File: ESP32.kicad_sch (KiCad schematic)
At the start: 33 parts, among them J2 Conn_01x04_Socket, U2 ESP32-C3FH4, U4 TS-1187A-B-A-B, U58 TS-1187A-B-A-B, U59 YTC-TC16-30, U60 AMS1117-3_3, X1 CF4040M00015001

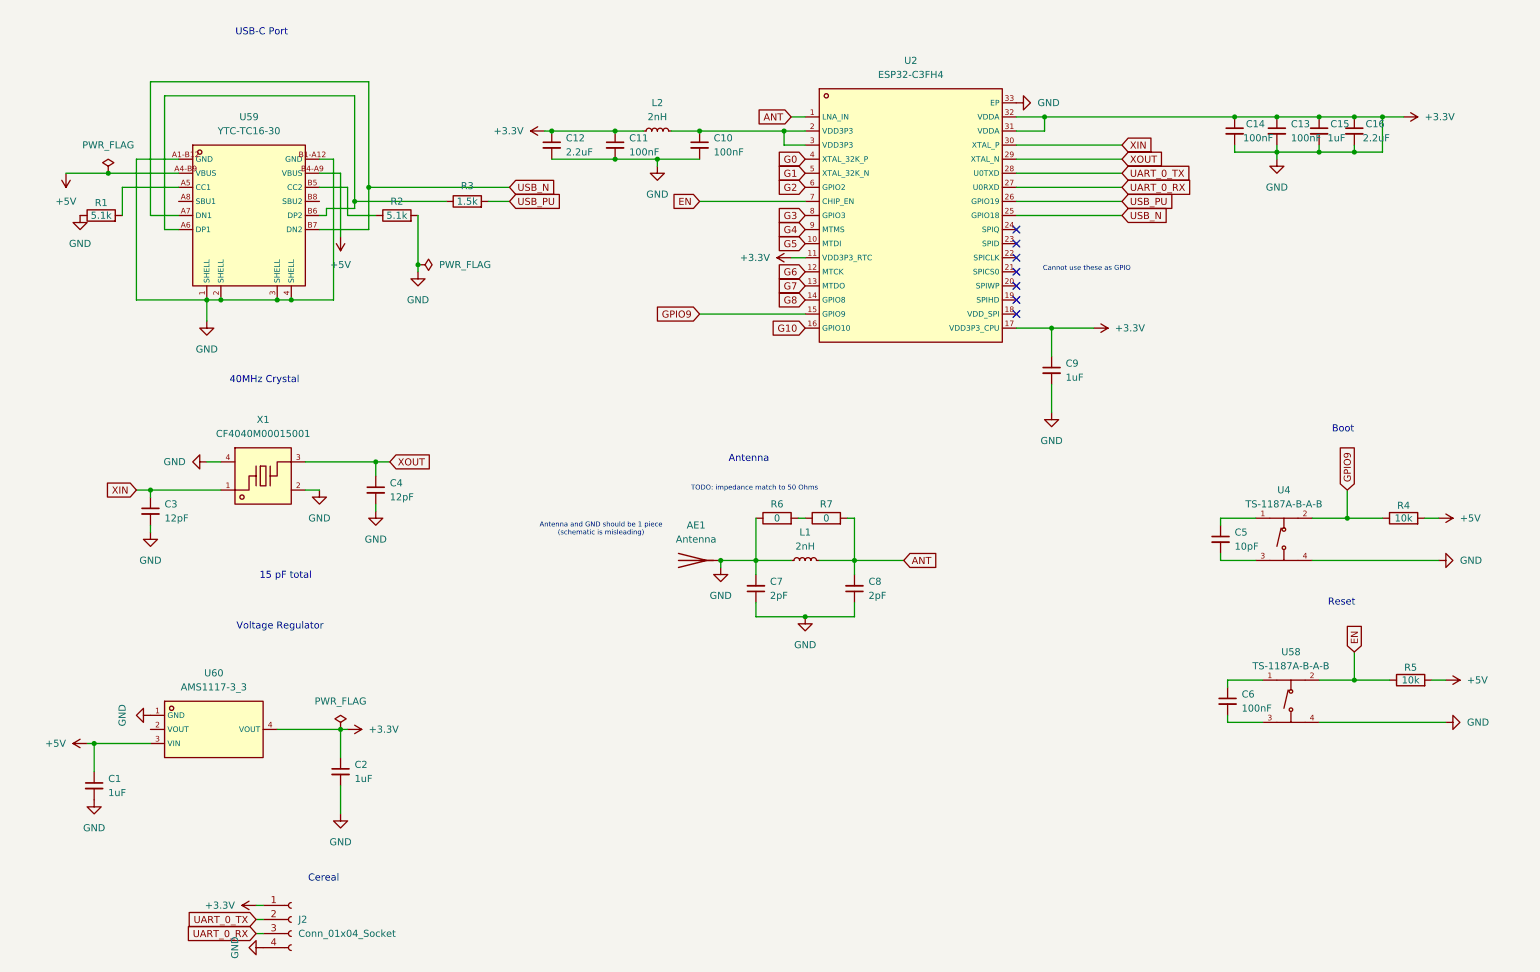
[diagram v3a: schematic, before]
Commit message: symbol fixes + placement
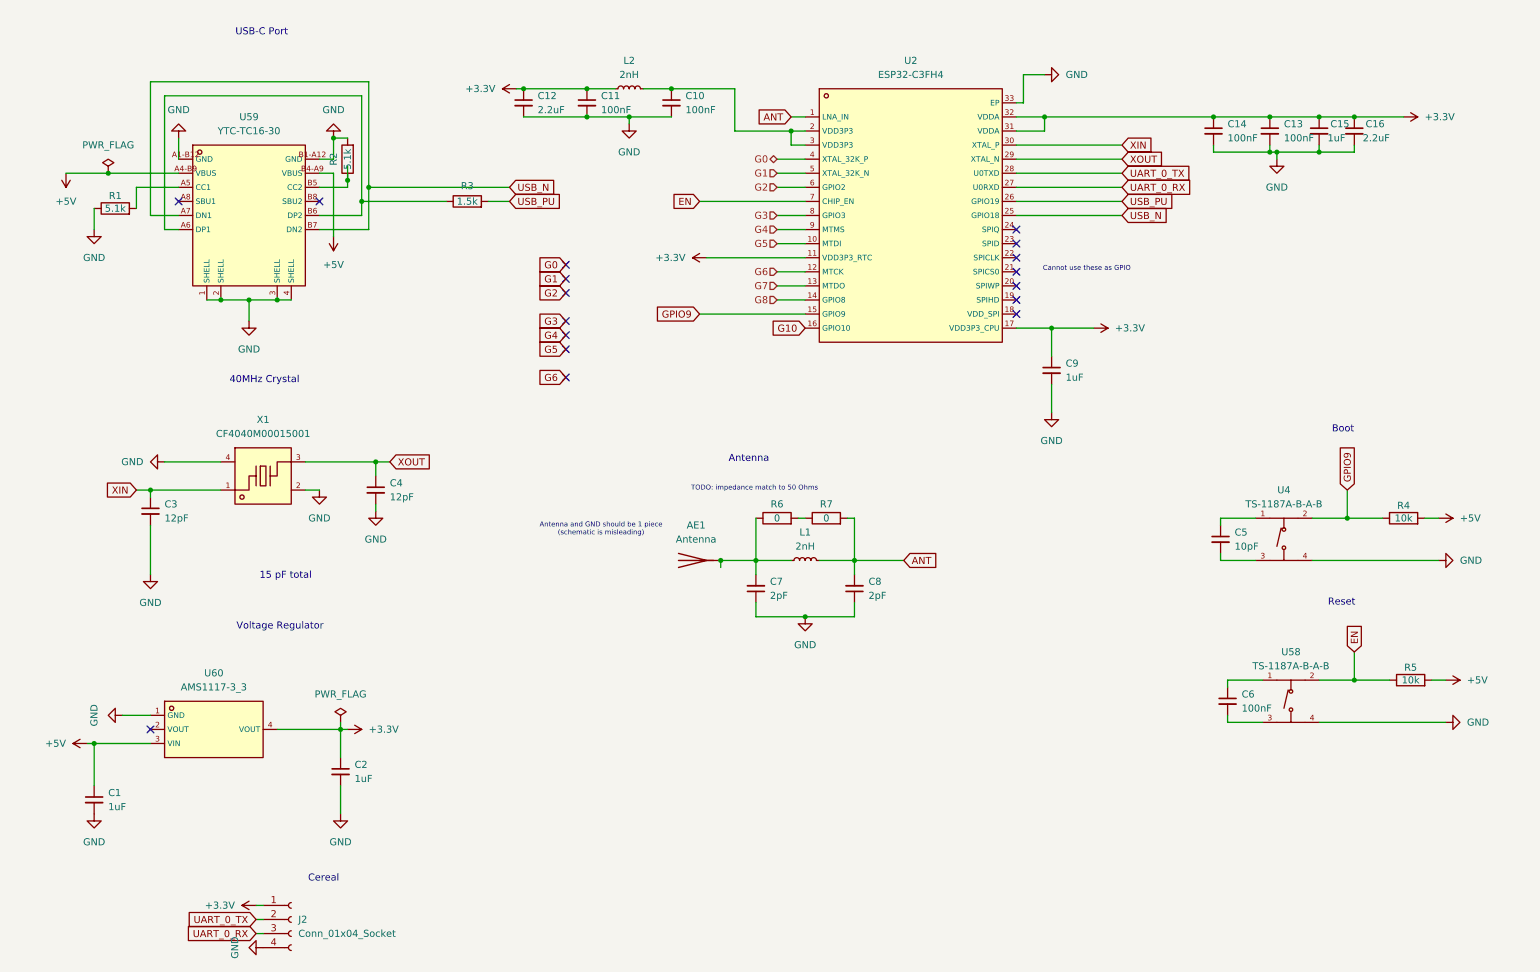
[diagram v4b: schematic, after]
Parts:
- AE1: footprint (none) -> ESP_Antenna:ESPRESSIF_ESP32_MIFA_2.4GHz_Right
- C1, C10, C11, C12, C13, C14, C15, C16, C2, C3, C4, C5, C6, C7, C8, C9: footprint (none) -> Capacitor_SMD:C_0402_1005Metric
- J2: footprint (none) -> Connector_PinHeader_2.54mm:PinHeader_1x04_P2.54mm_Vertical
- L1, L2: footprint (none) -> Inductor_SMD:L_0402_1005Metric
- R1, R2, R3, R4, R5, R6, R7: footprint (none) -> Resistor_SMD:R_0402_1005Metric
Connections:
- net +3.3V: no longer AE1.1 (A), C1.2, C10.2, C11.2, C12.2, C13.2, C14.2, C15.2, C16.2, C2.2, C3.2, C4.2, C7.1, C7.2, C8.1, C9.2, J2.4 (Pin_4), L1.1, R1.1, R2.2, R6.1, U2.33 (EP), U4.4 (D), U58.4 (D), U59.1 (SHELL), U59.2 (SHELL), U59.3 (SHELL), U59.4 (SHELL), U59.A1-B12 (GND), U59.B1-A12 (GND), U60.1 (GND), X1.2 (GND), X1.4 (GND)
- new net: AE1.1 (A), C7.2, L1.1, R6.1
- new net GND: C1.2, C10.2, C11.2, C12.2, C13.2, C14.2, C15.2, C16.2, C2.2, C3.2, C4.2, C7.1, C8.1, C9.2, J2.4 (Pin_4), R1.1, R2.2, U2.33 (EP), U4.4 (D), U58.4 (D), U59.1 (SHELL), U59.2 (SHELL), U59.3 (SHELL), U59.4 (SHELL), U59.A1-B12 (GND), U59.B1-A12 (GND), U60.1 (GND), X1.2 (GND), X1.4 (GND)
- no-connect marks 7 -> 17
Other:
- moved on the sheet: C1, C10, C12, L2, R1, R2

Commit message: Add PB_2, PB_8, switch antenna symbol to antenna shield
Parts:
- added C17, C18: 100nF, Capacitor_SMD:C_0402_1005Metric, symbol Device:C_Small
- added R8, R9: 10k, Resistor_SMD:R_0402_1005Metric, symbol Device:R
- added U5, U73: TS-1187A-B-A-B, footprint:SW-SMD_4P-L5.1-W5.1-P3.70-LS6.5-TL-2, symbol TS-1187A-B-A-B:TS-1187A-B-A-B
- AE1: symbol Device:Antenna -> Device:Antenna_Shield
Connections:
- net +5V: now also R8.2, R9.2
- net G2: no longer U2.6 (GPIO2)
- net GND: now also AE1.2 (Shield), U5.4 (D), U73.4 (D)
- net G8 renamed GPIO8
- net GPIO8: now also R9.1, U73.2 (B)
- new net: C18.1, U73.1 (A)
- new net: C18.2, U73.3 (C)
- new net: C17.1, U5.1 (A)
- new net: C17.2, U5.3 (C)
- new net GPIO2: R8.1, U2.6 (GPIO2), U5.2 (B)
- no-connect marks 17 -> 18
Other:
- note added: "PB_2"
- note added: "PB_8"
- note added: "Switches"
- moved on the sheet: C5, C6, R4, R5, U4, U58

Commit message: fixed LED matrix
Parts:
- added D1, D2: D, symbol Device:D
- added L3: 3.9nH, Inductor_SMD:L_0402_1005Metric, symbol Device:L_Small
- L2: value 2nH -> 3.9nH
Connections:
- net G7 is gone; now on net G6: U2.13 (MTDO)
- net +3.3V: now also D1.2 (A), L3.1; no longer U2.31 (VDDA), U2.32 (VDDA)
- net G2: now also U2.8 (GPIO3)
- net G3: now also U2.9 (MTMS); no longer U2.8 (GPIO3)
- net G4: now also U2.10 (MTDI); no longer U2.9 (MTMS)
- net G5: now also U2.12 (MTCK); no longer U2.10 (MTDI)
- net G6: no longer U2.12 (MTCK)
- net at C10.1, L2.2: now also D2.2 (A), L3.2; no longer U2.2 (VDD3P3), U2.3 (VDD3P3)
- new net: D1.1 (K), U2.31 (VDDA), U2.32 (VDDA)
- new net: D2.1 (K), U2.2 (VDD3P3), U2.3 (VDD3P3)
- no-connect marks 18 -> 10

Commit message: fixed LED matrix
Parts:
- removed D1: D, symbol Device:D
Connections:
- net +3.3V: now also U2.31 (VDDA), U2.32 (VDDA)
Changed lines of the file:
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@@
 	(wire
 		(pts
-			(xy 209.55 35.56) (xy 226.06 35.56)
-		)
-		(stroke
-			(width 0)
-			(type default)
-		)
-	)
-	(wire
-		(pts
 			(xy 52.07 68.58) (xy 52.07 72.39)
 		)
@@
 	(wire
 		(pts
-			(xy 195.58 35.56) (xy 201.93 35.56)
+			(xy 195.58 35.56) (xy 226.06 35.56)
 		)
 		(stroke
@@
 					(unit 1)
 				)
-			)
-		)
-	)
-	(symbol
-		(lib_id "Device:D")
-		(at 205.74 35.56 0)
-		(unit 1)
-		(exclude_from_sim no)
-		(in_bom yes)
-		(on_board yes)
-		(dnp no)
-		(fields_autoplaced yes)
-		(property "Reference" "D1"
-			(at 205.74 29.21 0)
-			(effects
-				(font
-					(size 1.27 1.27)
-				)
-			)
-		)
-		(property "Value" "D"
-			(at 205.74 31.75 0)
-			(effects
-				(font
-					(size 1.27 1.27)
-				)
-			)
-		)
-		(property "Footprint" ""
-			(at 205.74 35.56 0)
-			(effects
-				(font
-					(size 1.27 1.27)
-				)
-				(hide yes)
-			)
-		)
-		(property "Datasheet" "~"
-			(at 205.74 35.56 0)
-			(effects
-				(font
-					(size 1.27 1.27)
-				)
-				(hide yes)
-			)
-		)
-		(property "Description" "Diode"
-			(at 205.74 35.56 0)
-			(effects
-				(font
-					(size 1.27 1.27)
-				)
-				(hide yes)
-			)
-		)
-		(property "Sim.Device" "D"
-			(at 205.74 35.56 0)
-			(effects
-				(font
-					(size 1.27 1.27)
-				)
-				(hide yes)
-			)
-		)
-		(property "Sim.Pins" "1=K 2=A"
-			(at 205.74 35.56 0)
-			(effects
-				(font
-					(size 1.27 1.27)
-				)
-				(hide yes)
-			)
-		)
-		(pin "1"
-		)
-		(pin "2"
-		)
-		(instances
-			(project "esp-card"
-				(path "/93cf1a11-1660-4ae3-a523-02ca090cff0a/bb5d4e4a-cd64-4c06-bd3c-c3b86fee81c9"
-					(reference "D1")
-					(unit 1)
-				)

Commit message: better routing
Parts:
- removed D2: D, symbol Device:D
- L1: value 2nH -> 2.2nH
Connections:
- net at C10.1, L2.2, L3.2: now also U2.2 (VDD3P3), U2.3 (VDD3P3)
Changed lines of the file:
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@@
 	(wire
 		(pts
+			(xy 139.7 30.48) (xy 139.7 38.1)
+		)
+		(stroke
+			(width 0)
+			(type default)
+		)
+	)
+	(wire
+		(pts
 			(xy 124.46 30.48) (xy 128.27 30.48)
 		)
@@
 			)
 		)
-		(property "Value" "2nH"
+		(property "Value" "2.2nH"
 			(at 152.4 113.03 90)
 			(effects
@@
 					(unit 1)
 				)
-			)
-		)
-	)
-	(symbol
-		(lib_id "Device:D")
-		(at 139.7 34.29 90)
-		(unit 1)
-		(exclude_from_sim no)
-		(in_bom yes)
-		(on_board yes)
-		(dnp no)
-		(fields_autoplaced yes)
-		(property "Reference" "D2"
-			(at 142.24 33.0199 90)
-			(effects
-				(font
-					(size 1.27 1.27)
-				)
-				(justify right)
-			)
-		)
-		(property "Value" "D"
-			(at 142.24 35.5599 90)
-			(effects
-				(font
-					(size 1.27 1.27)
-				)
-				(justify right)
-			)
-		)
-		(property "Footprint" ""
-			(at 139.7 34.29 0)
-			(effects
-				(font
-					(size 1.27 1.27)
-				)
-				(hide yes)
-			)
-		)
-		(property "Datasheet" "~"
-			(at 139.7 34.29 0)
-			(effects
-				(font
-					(size 1.27 1.27)
-				)
-				(hide yes)
-			)
-		)
-		(property "Description" "Diode"
-			(at 139.7 34.29 0)
-			(effects
-				(font
-					(size 1.27 1.27)
-				)
-				(hide yes)
-			)
-		)
-		(property "Sim.Device" "D"
-			(at 139.7 34.29 0)
-			(effects
-				(font
-					(size 1.27 1.27)
-				)
-				(hide yes)
-			)
-		)
-		(property "Sim.Pins" "1=K 2=A"
-			(at 139.7 34.29 0)
-			(effects
-				(font
-					(size 1.27 1.27)
-				)
-				(hide yes)
-			)
-		)
-		(pin "1"
-		)
-		(pin "2"
-		)
-		(instances
-			(project "esp-card"
-				(path "/93cf1a11-1660-4ae3-a523-02ca090cff0a/bb5d4e4a-cd64-4c06-bd3c-c3b86fee81c9"
-					(reference "D2")
-					(unit 1)
-				)
